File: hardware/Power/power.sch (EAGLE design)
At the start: 42 parts, among them IC1 ACS712ELCTR-05B-T, IC2 LM358_SOIC, Q1 PNP, T1 ZMPT101B, X1 057-006-1

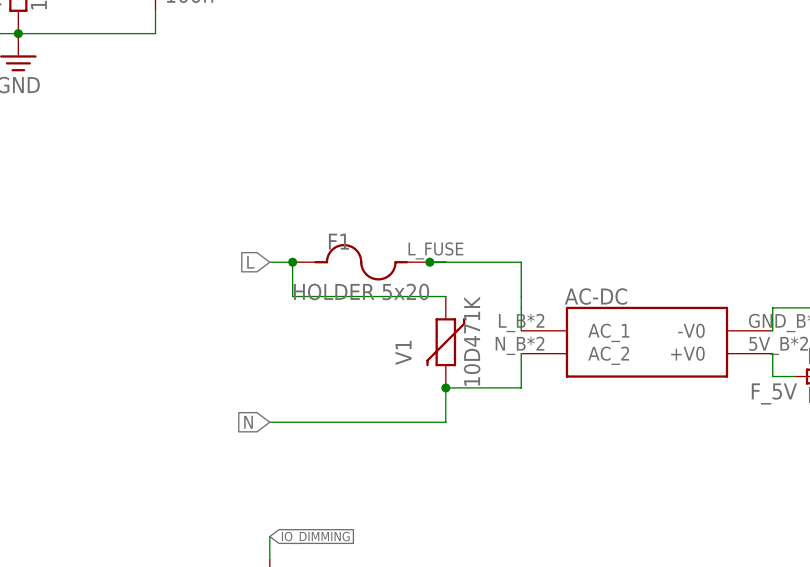
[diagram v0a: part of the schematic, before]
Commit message: fix : 2 layer pcb, dim pin terhalang
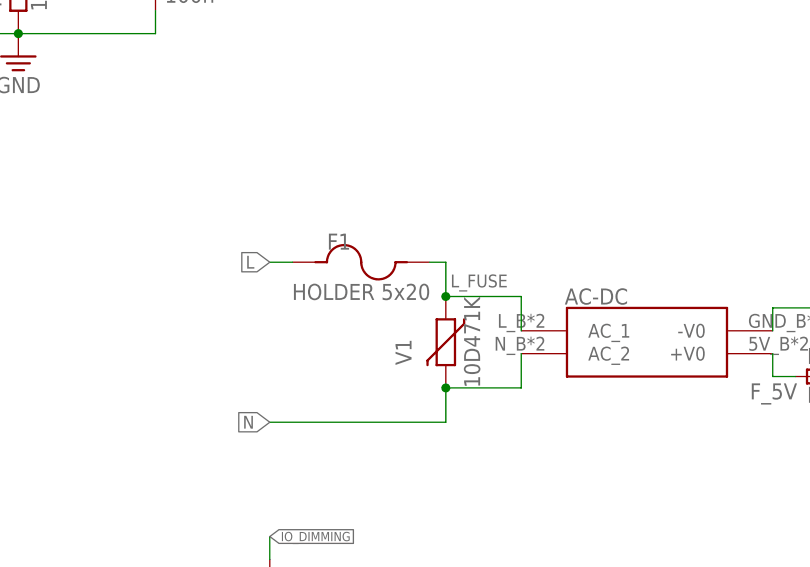
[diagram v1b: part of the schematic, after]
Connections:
- net L: no longer V1.1
- net L_FUSE: now also V1.1

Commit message: checkpoint 21/05
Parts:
- AC-DC: value HI-LINKVERTICAL -> HI-LINKAC-DC_3.5W(PTH); device XLKM#4:HI-LINKVERTICAL -> XLKM#4:HI-LINKAC-DC_3.5W(PTH)
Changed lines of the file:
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@@
 <grid distance="0.1" unitdist="inch" unit="inch" style="lines" multiple="1" display="no" altdistance="0.01" altunitdist="inch" altunit="inch"/>
 <layers>
-<layer number="1" name="Top" color="4" fill="1" visible="yes" active="no"/>
-<layer number="2" name="Route2" color="16" fill="1" visible="yes" active="no"/>
-<layer number="3" name="Route3" color="17" fill="1" visible="yes" active="no"/>
-<layer number="4" name="Route4" color="18" fill="1" visible="yes" active="no"/>
-<layer number="5" name="Route5" color="19" fill="1" visible="yes" active="no"/>
-<layer number="6" name="Route6" color="25" fill="1" visible="yes" active="no"/>
-<layer number="7" name="Route7" color="26" fill="1" visible="yes" active="no"/>
-<layer number="8" name="Route8" color="27" fill="1" visible="yes" active="no"/>
-<layer number="9" name="Route9" color="28" fill="1" visible="yes" active="no"/>
-<layer number="10" name="Route10" color="29" fill="1" visible="yes" active="no"/>
-<layer number="11" name="Route11" color="30" fill="1" visible="yes" active="no"/>
-<layer number="12" name="Route12" color="20" fill="1" visible="yes" active="no"/>
-<layer number="13" name="Route13" color="21" fill="1" visible="yes" active="no"/>
-<layer number="14" name="Route14" color="22" fill="1" visible="yes" active="no"/>
-<layer number="15" name="Route15" color="23" fill="1" visible="yes" active="no"/>
-<layer number="16" name="Bottom" color="1" fill="1" visible="yes" active="no"/>
-<layer number="17" name="Pads" color="2" fill="1" visible="yes" active="no"/>
-<layer number="18" name="Vias" color="2" fill="1" visible="yes" active="no"/>
-<layer number="19" name="Unrouted" color="6" fill="1" visible="yes" active="no"/>
-<layer number="20" name="Dimension" color="24" fill="1" visible="yes" active="no"/>
-<layer number="21" name="tPlace" color="7" fill="1" visible="yes" active="no"/>
-<layer number="22" name="bPlace" color="7" fill="1" visible="yes" active="no"/>
-<layer number="23" name="tOrigins" color="15" fill="1" visible="yes" active="no"/>
-<layer number="24" name="bOrigins" color="15" fill="1" visible="yes" active="no"/>
-<layer number="25" name="tNames" color="7" fill="1" visible="yes" active="no"/>
-<layer number="26" name="bNames" color="7" fill="1" visible="yes" active="no"/>
-<layer number="27" name="tValues" color="7" fill="1" visible="yes" active="no"/>
-<layer number="28" name="bValues" color="7" fill="1" visible="yes" active="no"/>
+<layer number="1" name="Top" color="4" fill="1" visible="no" active="no"/>
+<layer number="2" name="Route2" color="16" fill="1" visible="no" active="no"/>
+<layer number="3" name="Route3" color="17" fill="1" visible="no" active="no"/>
+<layer number="4" name="Route4" color="18" fill="1" visible="no" active="no"/>
+<layer number="5" name="Route5" color="19" fill="1" visible="no" active="no"/>
+<layer number="6" name="Route6" color="25" fill="1" visible="no" active="no"/>
+<layer number="7" name="Route7" color="26" fill="1" visible="no" active="no"/>
+<layer number="8" name="Route8" color="27" fill="1" visible="no" active="no"/>
+<layer number="9" name="Route9" color="28" fill="1" visible="no" active="no"/>
+<layer number="10" name="Route10" color="29" fill="1" visible="no" active="no"/>
+<layer number="11" name="Route11" color="30" fill="1" visible="no" active="no"/>
+<layer number="12" name="Route12" color="20" fill="1" visible="no" active="no"/>
+<layer number="13" name="Route13" color="21" fill="1" visible="no" active="no"/>
+<layer number="14" name="Route14" color="22" fill="1" visible="no" active="no"/>
+<layer number="15" name="Route15" color="23" fill="1" visible="no" active="no"/>
+<layer number="16" name="Bottom" color="1" fill="1" visible="no" active="no"/>
+<layer number="17" name="Pads" color="2" fill="1" visible="no" active="no"/>
+<layer number="18" name="Vias" color="2" fill="1" visible="no" active="no"/>
+<layer number="19" name="Unrouted" color="6" fill="1" visible="no" active="no"/>
+<layer number="20" name="Dimension" color="24" fill="1" visible="no" active="no"/>
+<layer number="21" name="tPlace" color="7" fill="1" visible="no" active="no"/>
+<layer number="22" name="bPlace" color="7" fill="1" visible="no" active="no"/>
+<layer number="23" name="tOrigins" color="15" fill="1" visible="no" active="no"/>
+<layer number="24" name="bOrigins" color="15" fill="1" visible="no" active="no"/>
+<layer number="25" name="tNames" color="7" fill="1" visible="no" active="no"/>
+<layer number="26" name="bNames" color="7" fill="1" visible="no" active="no"/>
+<layer number="27" name="tValues" color="7" fill="1" visible="no" active="no"/>
+<layer number="28" name="bValues" color="7" fill="1" visible="no" active="no"/>
 <layer number="29" name="tStop" color="7" fill="3" visible="no" active="no"/>
 <layer number="30" name="bStop" color="7" fill="6" visible="no" active="no"/>
@@
 <layer number="35" name="tGlue" color="7" fill="4" visible="no" active="no"/>
 <layer number="36" name="bGlue" color="7" fill="5" visible="no" active="no"/>
-<layer number="37" name="tTest" color="7" fill="1" visible="yes" active="no"/>
-<layer number="38" name="bTest" color="7" fill="1" visible="yes" active="no"/>
+<layer number="37" name="tTest" color="7" fill="1" visible="no" active="no"/>
+<layer number="38" name="bTest" color="7" fill="1" visible="no" active="no"/>
 <layer number="39" name="tKeepout" color="4" fill="11" visible="no" active="no"/>
 <layer number="40" name="bKeepout" color="1" fill="11" visible="no" active="no"/>
@@
 <layer number="44" name="Drills" color="7" fill="1" visible="no" active="no"/>
 <layer number="45" name="Holes" color="7" fill="1" visible="no" active="no"/>
-<layer number="46" name="Milling" color="3" fill="1" visible="yes" active="no"/>
-<layer number="47" name="Measures" color="7" fill="1" visible="yes" active="no"/>
-<layer number="48" name="Document" color="7" fill="1" visible="yes" active="no"/>
-<layer number="49" name="Reference" color="7" fill="1" visible="yes" active="no"/>
-<layer number="50" name="dxf" color="7" fill="1" visible="yes" active="no"/>
-<layer number="51" name="tDocu" color="7" fill="1" visible="yes" active="no"/>
-<layer number="52" name="bDocu" color="7" fill="1" visible="yes" active="no"/>
-<layer number="53" name="tGND_GNDA" color="7" fill="1" visible="yes" active="no"/>
-<layer number="54" name="bGND_GNDA" color="7" fill="1" visible="yes" active="no"/>
-<layer number="56" name="wert" color="7" fill="1" visible="yes" active="no"/>
-<layer number="57" name="t3D" color="7" fill="5" visible="yes" active="no"/>
-<layer number="58" name="b3D" color="7" fill="4" visible="yes" active="no"/>
-<layer number="59" name="tCarbon" color="7" fill="1" visible="yes" active="no"/>
-<layer number="60" name="bCarbon" color="7" fill="1" visible="yes" active="no"/>
+<layer number="46" name="Milling" color="3" fill="1" visible="no" active="no"/>
+<layer number="47" name="Measures" color="7" fill="1" visible="no" active="no"/>
+<layer number="48" name="Document" color="7" fill="1" visible="no" active="no"/>
+<layer number="49" name="Reference" color="7" fill="1" visible="no" active="no"/>
+<layer number="50" name="dxf" color="7" fill="1" visible="no" active="no"/>
+<layer number="51" name="tDocu" color="7" fill="1" visible="no" active="no"/>
+<layer number="52" name="bDocu" color="7" fill="1" visible="no" active="no"/>
+<layer number="53" name="tGND_GNDA" color="7" fill="1" visible="no" active="no"/>
+<layer number="54" name="bGND_GNDA" color="7" fill="1" visible="no" active="no"/>
+<layer number="56" name="wert" color="7" fill="1" visible="no" active="no"/>
+<layer number="57" name="t3D" color="7" fill="5" visible="no" active="no"/>
+<layer number="58" name="b3D" color="7" fill="4" visible="no" active="no"/>
+<layer number="59" name="tCarbon" color="7" fill="1" visible="no" active="no"/>
+<layer number="60" name="bCarbon" color="7" fill="1" visible="no" active="no"/>
 <layer number="88" name="SimResults" color="9" fill="1" visible="yes" active="yes"/>
 <layer number="89" name="SimProbes" color="9" fill="1" visible="yes" active="yes"/>
@@
 <part name="IC2" library="IC_Linear" library_urn="urn:adsk.eagle:library:16378340" deviceset="LM358" device="_SOIC" package3d_urn="urn:adsk.eagle:package:16378355/3"/>
 <part name="SUPPLY1" library="Power_Symbols" deviceset="GND-EARTH" device="" value="GND"/>
-<part name="AC-DC" library="XLKM#4" library_urn="urn:adsk.eagle:library:39528286" deviceset="HI-LINK" device="VERTICAL" package3d_urn="urn:adsk.eagle:package:39943964/3" value=""/>
+<part name="AC-DC" library="XLKM#4" library_urn="urn:adsk.eagle:library:39528286" deviceset="HI-LINK" device="AC-DC_3.5W(PTH)" package3d_urn="urn:adsk.eagle:package:40433506/2" value="HI-LINKAC-DC_3.5W(PTH)"/>
 <part name="C6" library="Capacitor" library_urn="urn:adsk.eagle:library:16290819" deviceset="C" device="CHIP-0805(2012-METRIC)" package3d_urn="urn:adsk.eagle:package:16290897/2" technology="_" value="1n"/>
 <part name="SUPPLY37" library="Power_Symbols" deviceset="GND-EARTH" device="" value="GND"/>
